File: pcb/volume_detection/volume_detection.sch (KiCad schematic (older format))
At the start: 16 parts, among them U1 MC34063AD

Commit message: finish schematic
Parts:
- added C4: 330nf, Capacitor_SMD:C_0805_2012Metric_Pad1.15x1.40mm_HandSolder, symbol Device:C
- added J1: Avr ISP, Connector_PinHeader_2.54mm:PinHeader_2x05_P2.54mm_Vertical, symbol Connector_Generic:Conn_02x05_Odd_Even
- added J2: Sens 1, TerminalBlock_MetzConnect:TerminalBlock_MetzConnect_Type055_RT01502HDWU_1x02_P5.00mm_Horizontal, symbol Connector:Screw_Terminal_01x02
- added J3: Sens 2, TerminalBlock_MetzConnect:TerminalBlock_MetzConnect_Type055_RT01502HDWU_1x02_P5.00mm_Horizontal, symbol Connector:Screw_Terminal_01x02
- added J4: +12v, TerminalBlock_MetzConnect:TerminalBlock_MetzConnect_Type055_RT01502HDWU_1x02_P5.00mm_Horizontal, symbol Connector:Screw_Terminal_01x02
- added R3, R6, R8: 10k, Resistor_SMD:R_0805_2012Metric_Pad1.15x1.40mm_HandSolder, symbol Device:R_Small
- added R7, R9: 250, Resistor_SMD:R_0805_2012Metric_Pad1.15x1.40mm_HandSolder, symbol Device:R_Small
- C1, C2, C3: renamed from C?; footprint (none) -> Capacitor_SMD:C_0805_2012Metric_Pad1.15x1.40mm_HandSolder
- Co1: renamed from Co; footprint (none) -> Capacitor_SMD:CP_Elec_4x5.4
- Ct1: renamed from Ct; footprint (none) -> Capacitor_SMD:C_0805_2012Metric_Pad1.15x1.40mm_HandSolder
- L1, L2: footprint (none) -> Inductor_THT:L_Axial_L5.3mm_D2.2mm_P10.16mm_Horizontal_Vishay_IM-1
- LCd1: renamed from LCd; footprint (none) -> Connector_PinHeader_2.54mm:PinHeader_1x16_P2.54mm_Vertical
- R1, R2: footprint (none) -> Resistor_SMD:R_0805_2012Metric_Pad1.15x1.40mm_HandSolder
- R4, R5: renamed from R?; footprint (none) -> Resistor_SMD:R_0805_2012Metric_Pad1.15x1.40mm_HandSolder
- Rsc1: renamed from Rsc; footprint (none) -> Resistor_SMD:R_0805_2012Metric_Pad1.15x1.40mm_HandSolder
- gave numbers to parts that had none: 1
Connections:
- net labels added: MISO, MOSI, RST, SCK, SEN1, SEN2
- wire segments 60 -> 108

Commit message: Finish pcb
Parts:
- R7, R9: value 250 -> 240
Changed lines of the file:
@@
 	4500 2000 4750 2000
 Text Label 4600 3200 0    50   ~ 0
+D7
+Text Label 4600 3300 0    50   ~ 0
+D6
+Text Label 4600 3400 0    50   ~ 0
+D5
+Text Label 4600 3500 0    50   ~ 0
+D4
+Text Label 4600 3600 0    50   ~ 0
+EN
+Text Label 4600 3700 0    50   ~ 0
 RS
-Text Label 4600 3300 0    50   ~ 0
-EN
-Text Label 4600 3400 0    50   ~ 0
-D4
-Text Label 4600 3500 0    50   ~ 0
-D5
-Text Label 4600 3600 0    50   ~ 0
-D6
-Text Label 4600 3700 0    50   ~ 0
-D7
 $Comp
 L power:GND #PWR0104
@@
 F 1 "10uF" H 3515 6555 50  0000 L CNN
 F 2 "Capacitor_SMD:CP_Elec_4x5.4" H 3438 6450 50  0001 C CNN
-F 3 "~" H 3400 6600 50  0001 C CNN
+F 3 "https://taydaelectronics.com/datasheets/files/a-1822.pdf" H 3400 6600 50  0001 C CNN
 	1    3400 6600
 	1    0    0    -1
@@
 P 9450 3200
 F 0 "R7" H 9509 3246 50  0000 L CNN
-F 1 "250" H 9509 3155 50  0000 L CNN
+F 1 "240" H 9509 3155 50  0000 L CNN
 F 2 "Resistor_SMD:R_0805_2012Metric_Pad1.15x1.40mm_HandSolder" H 9450 3200 50  0001 C CNN
 F 3 "~" H 9450 3200 50  0001 C CNN
@@
 P 9450 4550
 F 0 "R9" H 9509 4596 50  0000 L CNN
-F 1 "250" H 9509 4505 50  0000 L CNN
+F 1 "240" H 9509 4505 50  0000 L CNN
 F 2 "Resistor_SMD:R_0805_2012Metric_Pad1.15x1.40mm_HandSolder" H 9450 4550 50  0001 C CNN
 F 3 "~" H 9450 4550 50  0001 C CNN

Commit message: update pcb
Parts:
- C1, C3: value 100uf -> 100nf
- L1: footprint Inductor_THT:L_Axial_L5.3mm_D2.2mm_P10.16mm_Horizontal_Vishay_IM-1 -> Inductor_THT:L_Axial_L7.0mm_D3.3mm_P5.08mm_Vertical_Fastron_MICC
- L2: footprint Inductor_THT:L_Axial_L5.3mm_D2.2mm_P10.16mm_Horizontal_Vishay_IM-1 -> Inductor_THT:L_Axial_L6.6mm_D2.7mm_P10.16mm_Horizontal_Vishay_IM-2
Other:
- moved on the sheet: R1
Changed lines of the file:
@@
 P 2500 2100
 F 0 "C3" H 2615 2146 50  0000 L CNN
-F 1 "100uf" H 2615 2055 50  0000 L CNN
+F 1 "100nf" H 2615 2055 50  0000 L CNN
 F 2 "Capacitor_SMD:C_0805_2012Metric_Pad1.15x1.40mm_HandSolder" H 2538 1950 50  0001 C CNN
 F 3 "~" H 2500 2100 50  0001 C CNN
@@
 P 1700 5600
 F 0 "C1" H 1815 5646 50  0000 L CNN
-F 1 "100uf" H 1815 5555 50  0000 L CNN
+F 1 "100nf" H 1815 5555 50  0000 L CNN
 F 2 "Capacitor_SMD:C_0805_2012Metric_Pad1.15x1.40mm_HandSolder" H 1738 5450 50  0001 C CNN
 F 3 "~" H 1700 5600 50  0001 C CNN
@@
 L Device:R_Small R1
 U 1 1 5F38C4F4
-P 2900 6150
-F 0 "R1" H 2959 6196 50  0000 L CNN
-F 1 "1.2k" H 2959 6105 50  0000 L CNN
-F 2 "Resistor_SMD:R_0805_2012Metric_Pad1.15x1.40mm_HandSolder" H 2900 6150 50  0001 C CNN
-F 3 "~" H 2900 6150 50  0001 C CNN
-	1    2900 6150
-	1    0    0    -1
+P 2700 6350
+F 0 "R1" H 2759 6396 50  0000 L CNN
+F 1 "1.2k" H 2759 6305 50  0000 L CNN
+F 2 "Resistor_SMD:R_0805_2012Metric_Pad1.15x1.40mm_HandSolder" H 2700 6350 50  0001 C CNN
+F 3 "~" H 2700 6350 50  0001 C CNN
+	1    2700 6350
+	0    1    1    0
 $EndComp
 $Comp
@@
 F 0 "L1" V 3354 6178 50  0000 L CNN
 F 1 "150uH" V 3445 6178 50  0000 L CNN
-F 2 "Inductor_THT:L_Axial_L5.3mm_D2.2mm_P10.16mm_Horizontal_Vishay_IM-1" H 3400 6100 50  0001 C CNN
+F 2 "Inductor_THT:L_Axial_L7.0mm_D3.3mm_P5.08mm_Vertical_Fastron_MICC" H 3400 6100 50  0001 C CNN
 F 3 "~" H 3400 6100 50  0001 C CNN
 	1    3400 6100
@@
 F 0 "L2" H 3900 6565 50  0000 C CNN
 F 1 "1uH" H 3900 6474 50  0000 C CNN
-F 2 "Inductor_THT:L_Axial_L5.3mm_D2.2mm_P10.16mm_Horizontal_Vishay_IM-1" H 3900 6350 50  0001 C CNN
+F 2 "Inductor_THT:L_Axial_L6.6mm_D2.7mm_P10.16mm_Horizontal_Vishay_IM-2" H 3900 6350 50  0001 C CNN
 F 3 "~" H 3900 6350 50  0001 C CNN
 	1    3900 6350
@@
 	2900 5850 3150 5850
 Wire Wire Line
-	2900 5950 2900 6050
-Wire Wire Line
-	2900 6250 2900 6350
-Wire Wire Line
-	2900 6350 3000 6350
-Wire Wire Line
 	2500 6150 2500 6350
-Wire Wire Line
-	2900 6350 2500 6350
-Connection ~ 2900 6350
 Connection ~ 2500 6350
 Wire Wire Line
@@
 Wire Wire Line
 	1400 1300 1400 1400
+Wire Wire Line
+	2600 6350 2500 6350
+Wire Wire Line
+	2800 6350 2900 6350
+Wire Wire Line
+	2900 5950 2900 6350
+Connection ~ 2900 6350
+Wire Wire Line
+	2900 6350 3000 6350
 $EndSCHEMATC

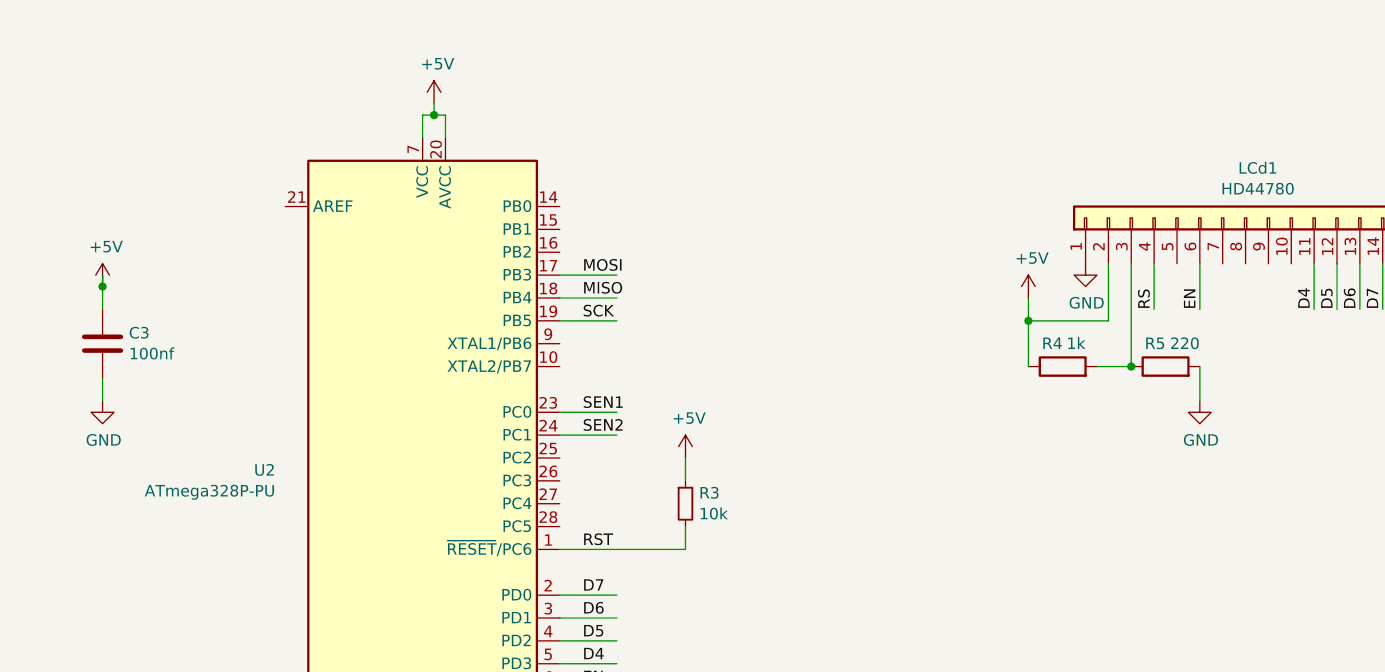
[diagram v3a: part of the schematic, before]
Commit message: update pcb + adc driver
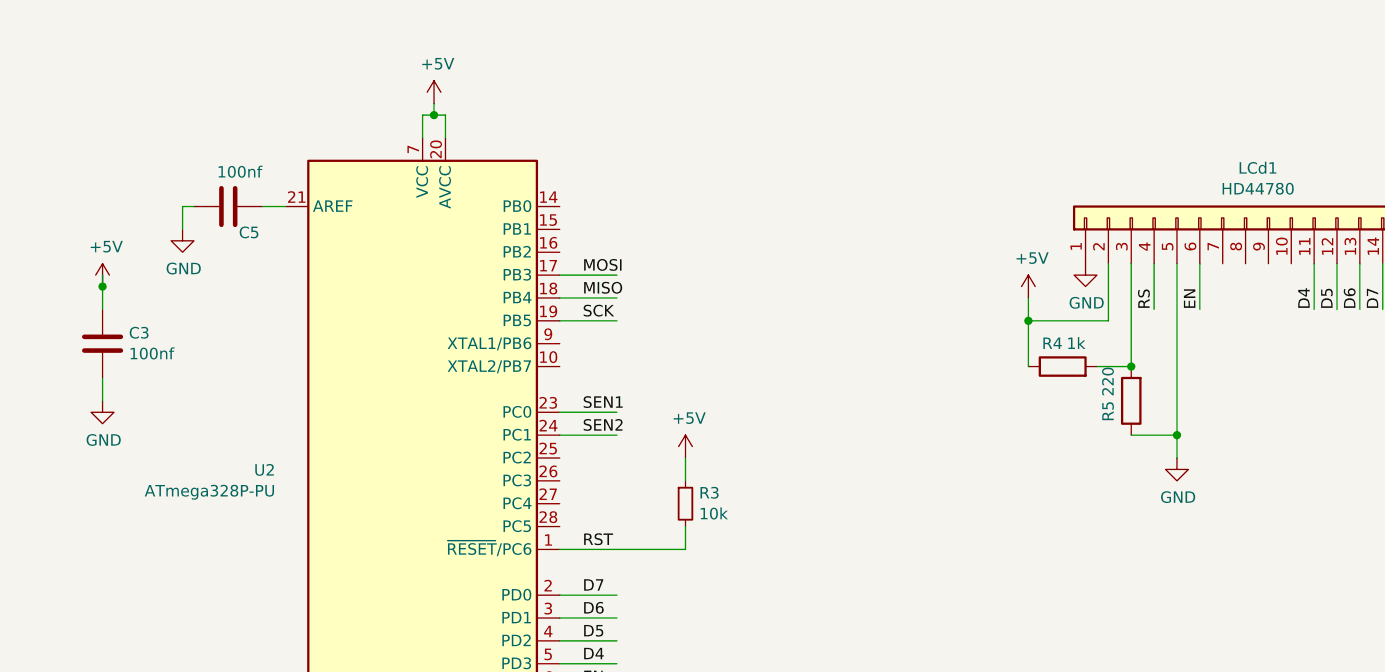
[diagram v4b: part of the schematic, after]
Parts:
- added C5: 100nf, Capacitor_SMD:C_0805_2012Metric_Pad1.15x1.40mm_HandSolder, symbol Device:C
- J1: footprint Connector_PinHeader_2.54mm:PinHeader_2x05_P2.54mm_Vertical -> Connector_PinHeader_2.54mm:PinHeader_2x05_P2.54mm_Horizontal
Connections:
- wire segments 108 -> 113
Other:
- moved on the sheet: R5
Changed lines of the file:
@@
 L power:GND #PWR0101
 U 1 1 5F34BC92
-P 7300 2350
-F 0 "#PWR0101" H 7300 2100 50  0001 C CNN
-F 1 "GND" H 7305 2177 50  0000 C CNN
-F 2 "" H 7300 2350 50  0001 C CNN
-F 3 "" H 7300 2350 50  0001 C CNN
-	1    7300 2350
+P 7200 2600
+F 0 "#PWR0101" H 7200 2350 50  0001 C CNN
+F 1 "GND" H 7205 2427 50  0000 C CNN
+F 2 "" H 7200 2600 50  0001 C CNN
+F 3 "" H 7200 2600 50  0001 C CNN
+	1    7200 2600
 	1    0    0    -1
 $EndComp
@@
 L Device:R R5
 U 1 1 5F34FD8B
-P 7150 2200
-F 0 "R5" V 7250 2200 50  0000 L CNN
-F 1 "220" V 7250 2050 50  0000 L CNN
-F 2 "Resistor_SMD:R_0805_2012Metric_Pad1.15x1.40mm_HandSolder" V 7080 2200 50  0001 C CNN
-F 3 "~" H 7150 2200 50  0001 C CNN
-	1    7150 2200
-	0    -1   -1   0
+P 7000 2350
+F 0 "R5" V 7100 2350 50  0000 L CNN
+F 1 "220" V 7100 2200 50  0000 L CNN
+F 2 "Resistor_SMD:R_0805_2012Metric_Pad1.15x1.40mm_HandSolder" V 6930 2350 50  0001 C CNN
+F 3 "~" H 7000 2350 50  0001 C CNN
+	1    7000 2350
+	-1   0    0    1
 $EndComp
 $Comp
@@
 Wire Wire Line
 	6850 2200 7000 2200
-Connection ~ 7000 2200
 Wire Wire Line
 	7000 1750 7000 2200
@@
 Wire Wire Line
 	6550 2000 6550 2200
-Wire Wire Line
-	7300 2200 7300 2350
 Wire Wire Line
 	7100 1750 7100 1950
@@
 F 0 "J1" H 6950 5167 50  0000 C CNN
 F 1 "Avr ISP" H 6950 5076 50  0000 C CNN
-F 2 "Connector_PinHeader_2.54mm:PinHeader_2x05_P2.54mm_Vertical" H 6900 4750 50  0001 C CNN
+F 2 "Connector_PinHeader_2.54mm:PinHeader_2x05_P2.54mm_Horizontal" H 6900 4750 50  0001 C CNN
 F 3 "~" H 6900 4750 50  0001 C CNN
 	1    6900 4750
@@
 Wire Wire Line
 	2900 6350 3000 6350
+Connection ~ 7000 2200
+Wire Wire Line
+	7000 2500 7200 2500
+Wire Wire Line
+	7200 2500 7200 2600
+Wire Wire Line
+	7200 1750 7200 2500
+Connection ~ 7200 2500
+$Comp
+L Device:C C5
+U 1 1 5F550C42
+P 3050 1500
+F 0 "C5" V 3165 1546 50  0000 L CNN
+F 1 "100nf" V 2900 1450 50  0000 L CNN
+F 2 "Capacitor_SMD:C_0805_2012Metric_Pad1.15x1.40mm_HandSolder" H 3088 1350 50  0001 C CNN
+F 3 "~" H 3050 1500 50  0001 C CNN
+	1    3050 1500
+	0    1    1    0
+$EndComp
+Wire Wire Line
+	3200 1500 3300 1500
+$Comp
+L power:GND #PWR0123
+U 1 1 5F5559DB
+P 2850 1600
+F 0 "#PWR0123" H 2850 1350 50  0001 C CNN
+F 1 "GND" H 2855 1427 50  0000 C CNN
+F 2 "" H 2850 1600 50  0001 C CNN
+F 3 "" H 2850 1600 50  0001 C CNN
+	1    2850 1600
+	1    0    0    -1
+$EndComp
+Wire Wire Line
+	2850 1600 2850 1500
+Wire Wire Line
+	2850 1500 2900 1500
 $EndSCHEMATC
